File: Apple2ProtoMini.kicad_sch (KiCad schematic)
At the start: 2 parts, among them J1 Apple II Bus Card Edge, J2 Apple II Bus Card Pin Header

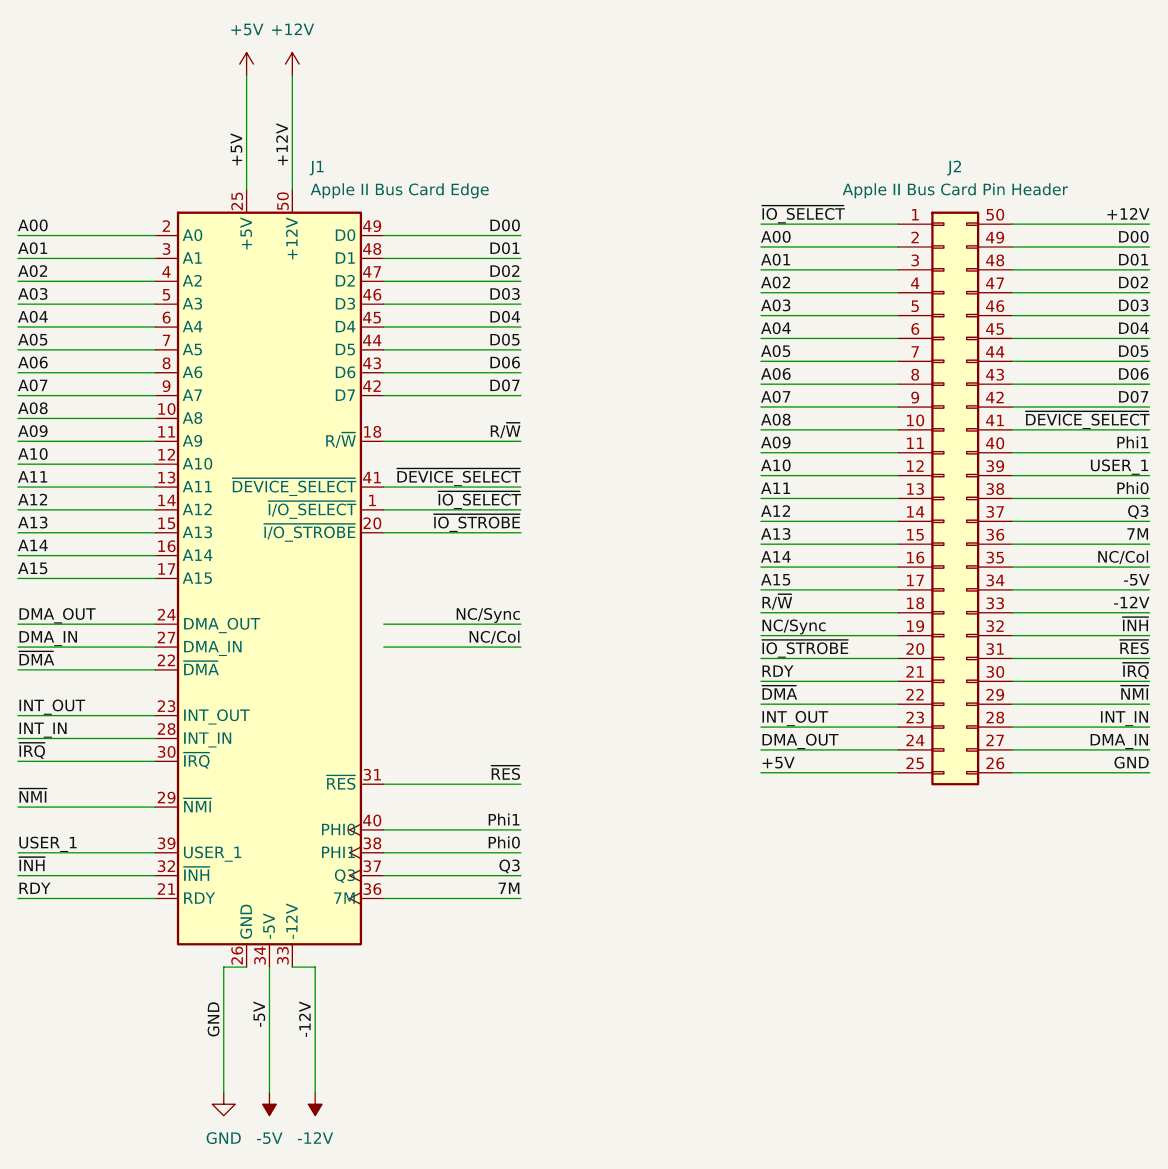
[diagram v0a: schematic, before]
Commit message: Added Midsized 7" board. Found spec on Apple II Expansion Card sizes (adding to repo). Updated all boards to be within spec (mostly).
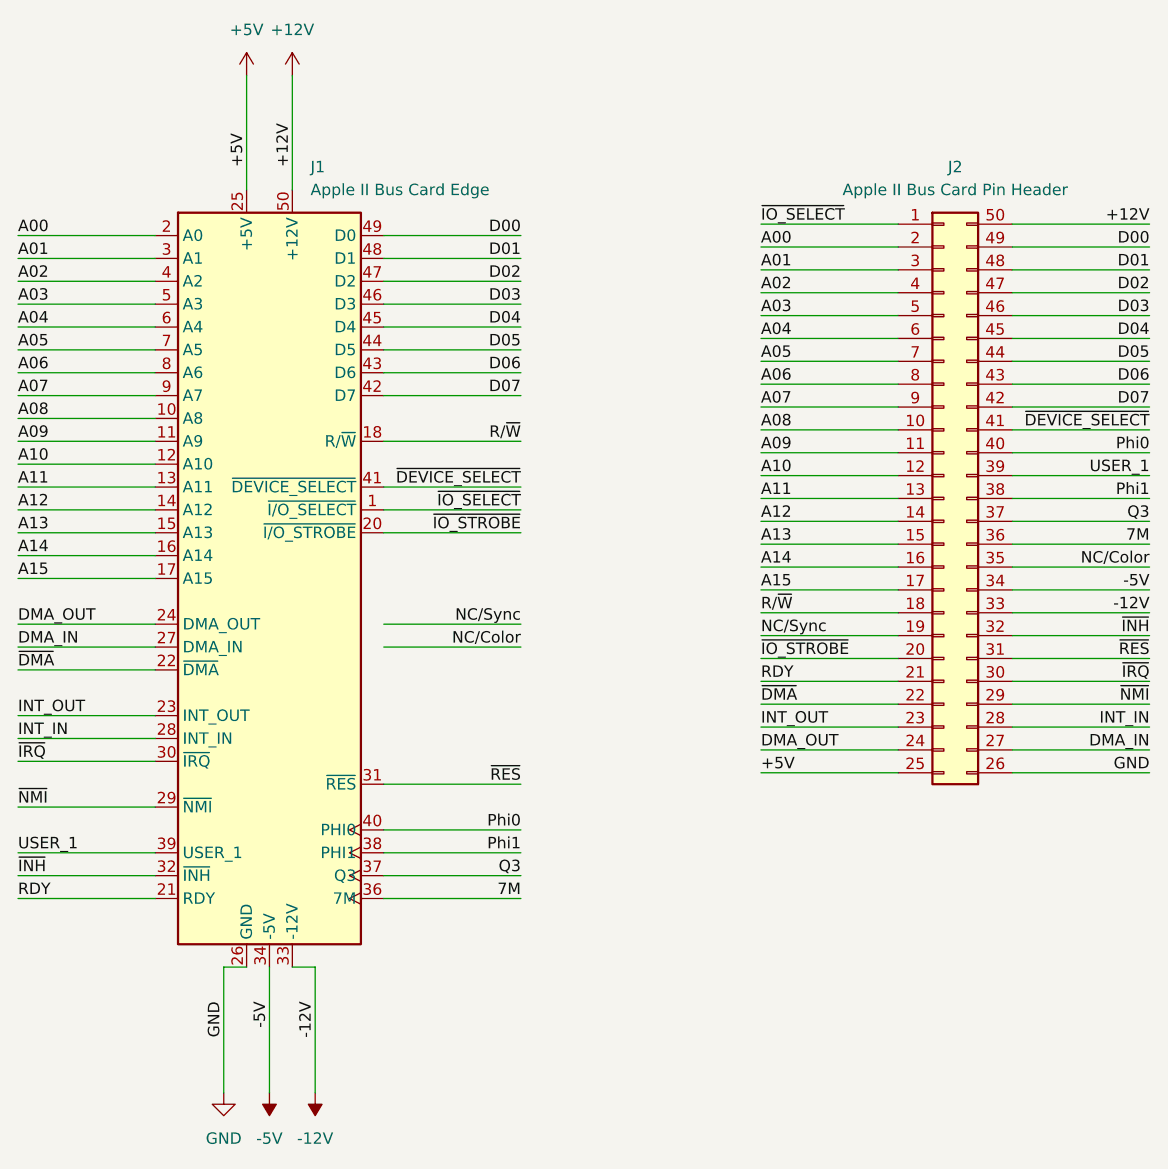
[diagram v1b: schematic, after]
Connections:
- net Phi0: now also J1.40 (PHI0), J2.40 (Pin_40); no longer J1.38 (PHI1), J2.38 (Pin_38)
- net Phi1: now also J1.38 (PHI1), J2.38 (Pin_38); no longer J1.40 (PHI0), J2.40 (Pin_40)
- net NC/Col renamed NC/Color
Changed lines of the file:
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@@
     (effects (font (size 1.27 1.27)) (justify left bottom))
   )
-  (label "Phi1" (at 142.24 128.27 180)
+  (label "Phi0" (at 142.24 128.27 180)
     (effects (font (size 1.27 1.27)) (justify right bottom))
   )
@@
     (effects (font (size 1.27 1.27)) (justify right bottom))
   )
-  (label "NC{slash}Col" (at 212.09 99.06 180)
+  (label "NC{slash}Color" (at 212.09 99.06 180)
     (effects (font (size 1.27 1.27)) (justify right bottom))
   )
@@
     (effects (font (size 1.27 1.27)) (justify left bottom))
   )
-  (label "NC{slash}Col" (at 142.24 107.95 180)
+  (label "NC{slash}Color" (at 142.24 107.95 180)
     (effects (font (size 1.27 1.27)) (justify right bottom))
   )
@@
     (effects (font (size 1.27 1.27)) (justify left bottom))
   )
-  (label "Phi0" (at 212.09 91.44 180)
+  (label "Phi1" (at 212.09 91.44 180)
     (effects (font (size 1.27 1.27)) (justify right bottom))
   )
@@
     (effects (font (size 1.27 1.27)) (justify left bottom))
   )
-  (label "Phi0" (at 142.24 130.81 180)
+  (label "Phi1" (at 142.24 130.81 180)
     (effects (font (size 1.27 1.27)) (justify right bottom))
   )
@@
     (effects (font (size 1.27 1.27)) (justify left bottom))
   )
-  (label "Phi1" (at 212.09 86.36 180)
-    (effects (font (size 1.27 1.27)) (justify right bottom))
-  )
+  (label "Phi0" (at 212.09 86.36 180)
+    (effects (font (size 1.27 1.27)) (justify right bottom))
+  )
